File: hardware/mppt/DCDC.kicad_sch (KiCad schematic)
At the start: 32 parts, among them Q501 EPC2059, Q502 EPC2059

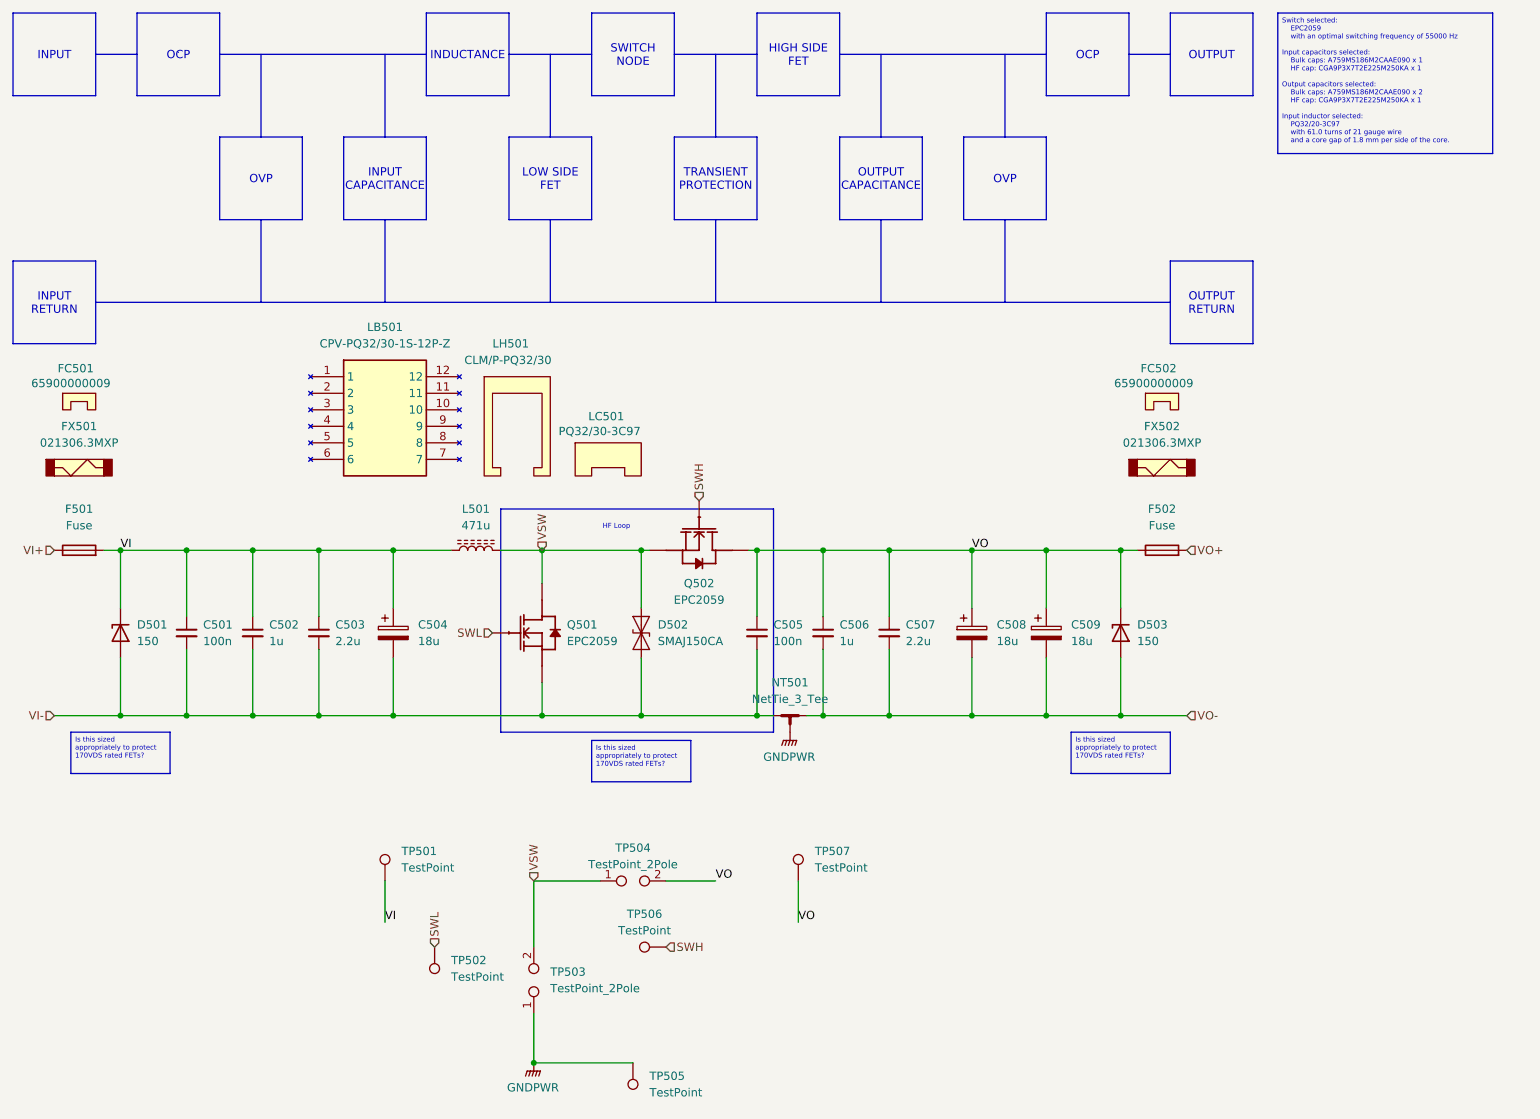
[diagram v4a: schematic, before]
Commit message: PCB variant for power regulation breakout.
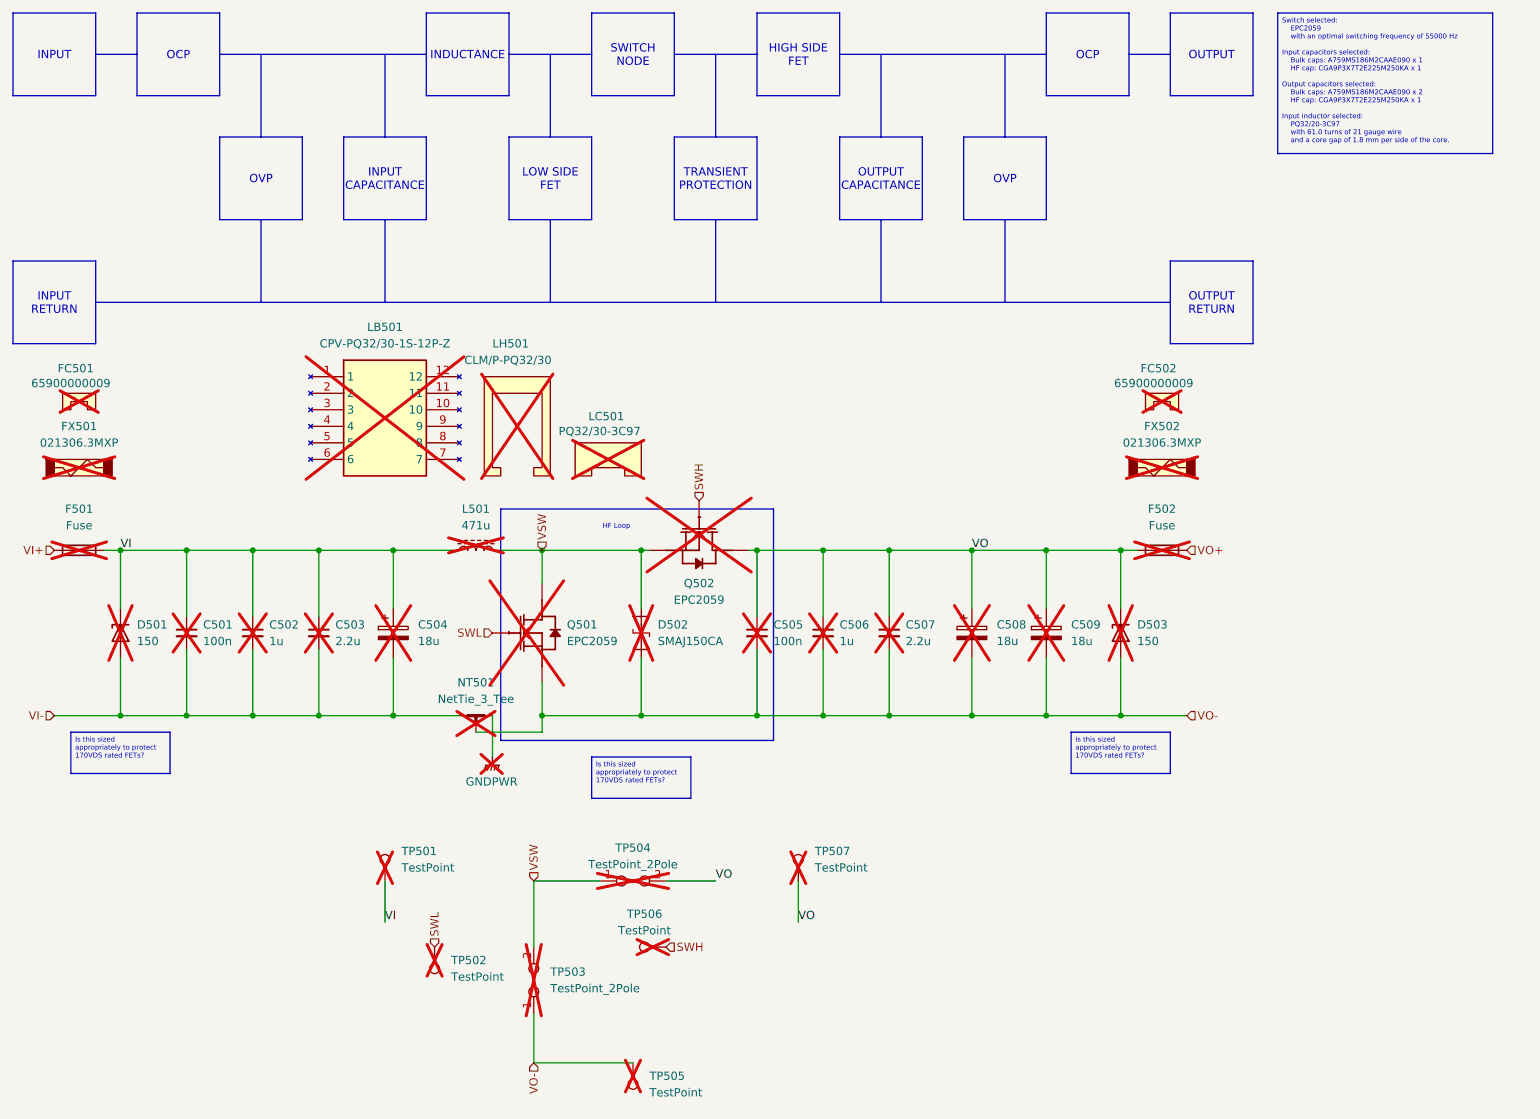
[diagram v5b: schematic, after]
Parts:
- C501, C502, C503, C504, C505, C506, C507, C508, C509, F501, F502, FC501, FC502, FX501, FX502, L501, LB501, LC501, LH501, Q501, Q502, TP501, TP502, TP503, TP504, TP505, TP506, TP507: now not fitted; now left out of the parts list
- D501, D502, D503: footprint Diode_SMD:D_SMA_Handsoldering -> Diode_SMD:D_SMA; now not fitted; now left out of the parts list
- NT501: now not fitted
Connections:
- net GNDPWR: now also NT501.2; no longer NT501.3, TP503.1, TP505.1
- net VI-: no longer C505.2, D502.1 (A1), Q501.2 (S), Q501.4 (S), Q501.6 (S)
- net VO-: now also C505.2, D502.1 (A1), NT501.3, Q501.2 (S), Q501.4 (S), Q501.6 (S), TP503.1, TP505.1; no longer NT501.2

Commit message: converter schematic and layout.
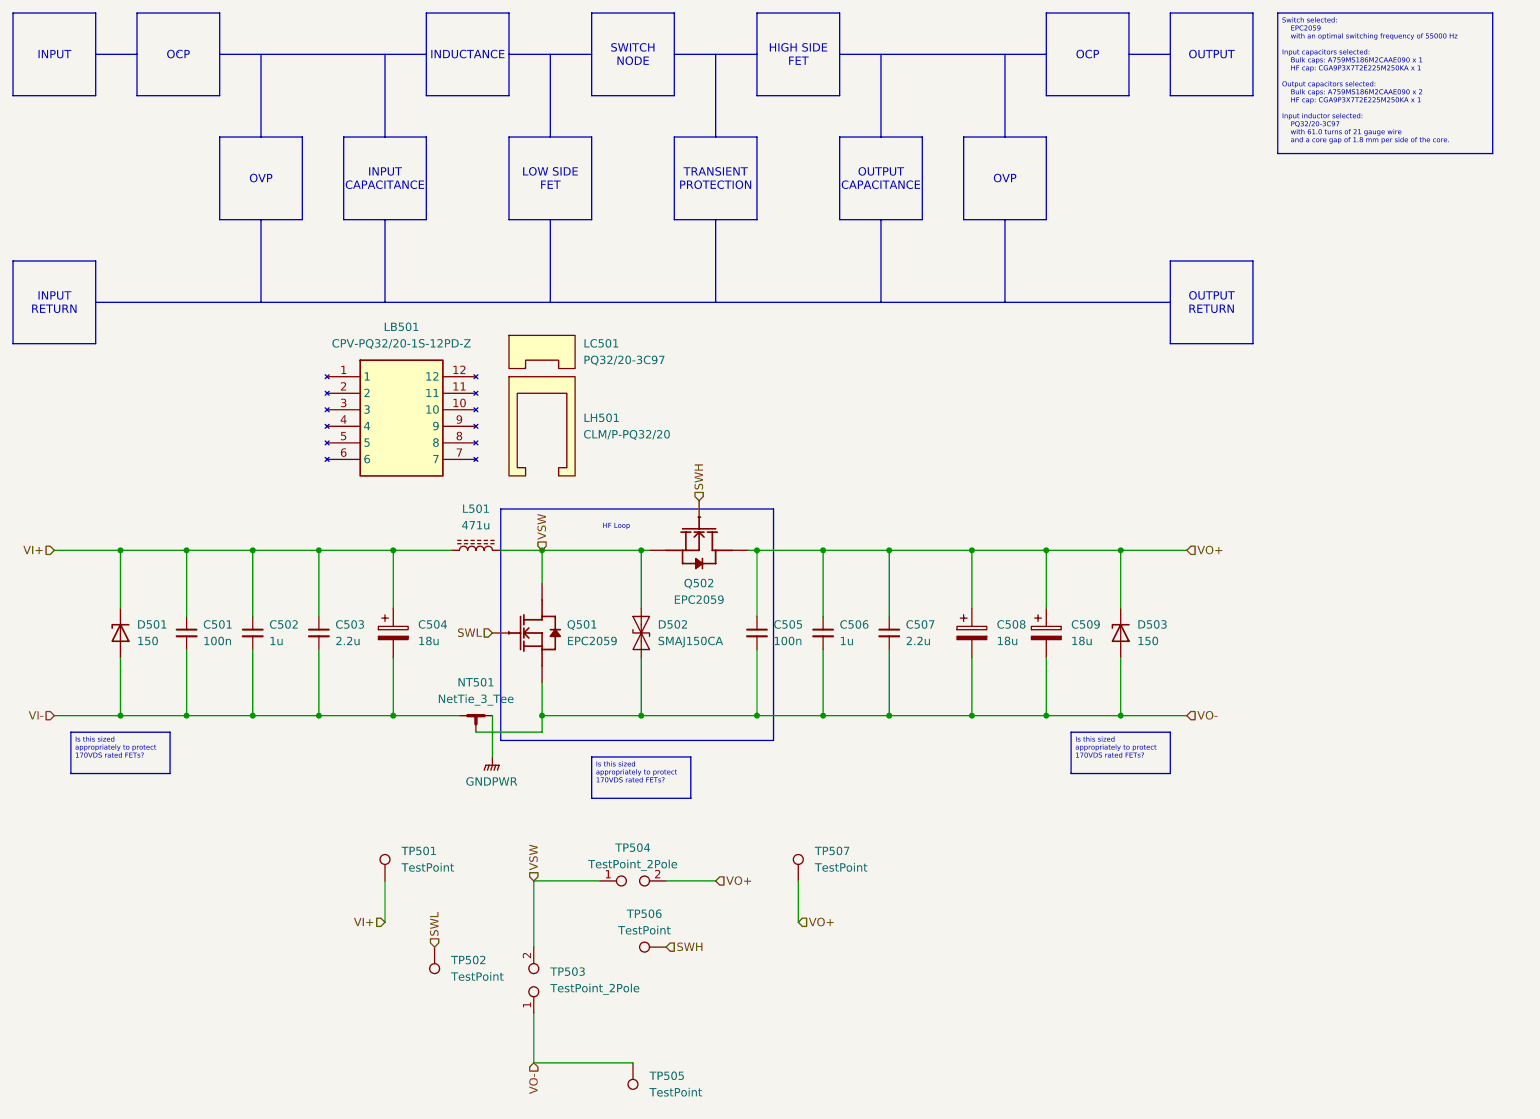
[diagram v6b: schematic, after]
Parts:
- removed F501, F502: Fuse, footprints:littelfuse_65600001009, symbol Device:Fuse
- removed FC501, FC502: 65900000009, symbol littelfuse_021306_3MXP:65900000009
- removed FX501, FX502: 021306.3MXP, symbol littelfuse_021306_3MXP:021306_3MXP
- removed LB501: CPV-PQ32/30-1S-12P-Z, footprints:ferroxcube_CPV-PQ32_30-1S-12P-Z, symbol ferroxcube_PQ32_30_3C97:CPV-PQ32/30-1S-12P-Z
- removed LC501: PQ32/30-3C97, symbol ferroxcube_PQ32_30_3C97:PQ32/30-3C97
- removed LH501: CLM/P-PQ32/30, symbol ferroxcube_PQ32_30_3C97:CLM/P-PQ32/30
- added LB501: CPV-PQ32/20-1S-12PD-Z, footprints:ferroxcube_CPV-PQ32_20-1S-12P-Z, symbol ferroxcube_PQ32_20_3C97:CPV-PQ32/20-1S-12P-Z
- added LC501: PQ32/20-3C97, symbol ferroxcube_PQ32_20_3C97:PQ32/20-3C97
- added LH501: CLM/P-PQ32/20, symbol ferroxcube_PQ32_20_3C97:CLM/P-PQ32/30
- C501, C502, C503, C504, C505, C506, C507, C508, C509, D501, D502, D503, NT501, Q501, Q502, TP501, TP502, TP503, TP504, TP505, TP506, TP507: now fitted; now in the parts list
- L501: footprint footprints:ferroxcube_PQ32_30_3C97_wire -> footprints:ferroxcube_PQ32_20_3C97_wire; now fitted; now in the parts list
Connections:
- net VI is gone; now on net VI+: C501.1, C502.1, C503.1, C504.1, D501.1 (K), L501.1, TP501.1
- net VO is gone; now on net VO+: C505.1, C506.1, C507.1, C508.1, C509.1, D503.1 (K), Q502.3 (D), Q502.5 (D), TP504.2, TP507.1

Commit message: remove testpoints, integrat 60% of layout
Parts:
- C501, C505: footprint Capacitor_SMD:C_1206_3216Metric_Pad1.33x1.80mm_HandSolder -> Capacitor_SMD:C_0805_2012Metric; Notes 85V Rating -> 200V Rating; P/N CGA5L3X7R2E104K160AA -> CGA4J3X7T2E104K125AA
- C502, C503, C506, C507: footprint Capacitor_SMD:C_2220_5750Metric_Pad1.97x5.40mm_HandSolder -> Capacitor_SMD:C_2220_5750Metric; Notes 150V Rating -> 200V Rating
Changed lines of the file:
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@@
 			)
 		)
-		(property "Footprint" "Capacitor_SMD:C_1206_3216Metric_Pad1.33x1.80mm_HandSolder"
+		(property "Footprint" "Capacitor_SMD:C_0805_2012Metric"
 			(at 45.72 114.3 0)
 			(effects
@@
 			)
 		)
-		(property "Datasheet" "https://product.tdk.com/en/search/capacitor/ceramic/mlcc/info?part_no=CGA5L3X7R2E104K160AA"
+		(property "Datasheet" "https://product.tdk.com/en/search/capacitor/ceramic/mlcc/info?part_no=CGA4J3X7T2E104K125AA"
 			(at 45.72 114.3 0)
 			(effects
@@
 			)
 		)
-		(property "P/N" "CGA5L3X7R2E104K160AA "
+		(property "P/N" "CGA4J3X7T2E104K125AA "
 			(at 45.72 114.3 0)
 			(effects
@@
 			)
 		)
-		(property "Notes" "85V Rating"
+		(property "Notes" "200V Rating"
 			(at 45.72 114.3 0)
 			(effects
@@
 			)
 		)
-		(property "Footprint" "Capacitor_SMD:C_2220_5750Metric_Pad1.97x5.40mm_HandSolder"
+		(property "Footprint" "Capacitor_SMD:C_2220_5750Metric"
 			(at 153.67 114.3 0)
 			(effects
@@
 			)
 		)
-		(property "Notes" "150V Rating"
+		(property "Notes" "200V Rating"
 			(at 153.67 114.3 0)
 			(effects
@@
 			)
 		)
-		(property "Footprint" "Capacitor_SMD:C_1206_3216Metric_Pad1.33x1.80mm_HandSolder"
+		(property "Footprint" "Capacitor_SMD:C_0805_2012Metric"
 			(at 133.35 114.3 0)
 			(effects
@@
 			)
 		)
-		(property "Datasheet" "https://product.tdk.com/en/search/capacitor/ceramic/mlcc/info?part_no=CGA5L3X7R2E104K160AA"
+		(property "Datasheet" "https://product.tdk.com/en/search/capacitor/ceramic/mlcc/info?part_no=CGA4J3X7T2E104K125AA"
 			(at 133.35 114.3 0)
 			(effects
@@
 			)
 		)
-		(property "P/N" "CGA5L3X7R2E104K160AA "
+		(property "P/N" "CGA4J3X7T2E104K125AA "
 			(at 133.35 114.3 0)
 			(effects
@@
 			)
 		)
-		(property "Notes" "85V Rating"
+		(property "Notes" "200V Rating"
 			(at 133.35 114.3 0)
 			(effects
@@
 			)
 		)
-		(property "Footprint" "Capacitor_SMD:C_2220_5750Metric_Pad1.97x5.40mm_HandSolder"
+		(property "Footprint" "Capacitor_SMD:C_2220_5750Metric"
 			(at 55.88 114.3 0)
 			(effects
@@
 			)
 		)
-		(property "Notes" "150V Rating"
+		(property "Notes" "200V Rating"
 			(at 55.88 114.3 0)
 			(effects
@@
 			)
 		)
-		(property "Footprint" "Capacitor_SMD:C_2220_5750Metric_Pad1.97x5.40mm_HandSolder"
+		(property "Footprint" "Capacitor_SMD:C_2220_5750Metric"
 			(at 66.04 114.3 0)
 			(effects
@@
 			)
 		)
-		(property "Notes" "150V Rating"
+		(property "Notes" "200V Rating"
 			(at 66.04 114.3 0)
 			(effects
@@
 			)
 		)
-		(property "Footprint" "Capacitor_SMD:C_2220_5750Metric_Pad1.97x5.40mm_HandSolder"
+		(property "Footprint" "Capacitor_SMD:C_2220_5750Metric"
 			(at 143.51 114.3 0)
 			(effects
@@
 			)
 		)
-		(property "Notes" "150V Rating"
+		(property "Notes" "200V Rating"
 			(at 143.51 114.3 0)
 			(effects
